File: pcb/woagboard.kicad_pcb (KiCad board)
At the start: 2 copper layers, 134.6 x 108.6 mm, 74 parts, among them J10 Flash connection, J2 HRO_TYPE-C-31-M-14, J3 Battery JST, Q2 2N7002, SW1 SW_Push, SW10 SW_Push, SW11 SW_Push, SW12 SW_Push, SW13 SW_Push, SW14 SW_Push, SW15 SW_Push, SW16 SW_Push, SW17 SW_Push, SW18 SW_Push, SW2 SW_Push, SW3 SW_Push, SW4 SW_Push, SW5 SW_Push, SW6 SW_Push, SW7 SW_Push, SW8 SW_Push, SW9 SW_Push, U1 SRV05-4, U10 MAX17048, U3 BQ24075, U9 nRF52840_E73-2G4M08S1C, Y1 32.768 KHz

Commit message: wip: finish left half and start work on right half
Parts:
- removed C17: 100n, Capacitor_SMD:C_0402_1005Metric
- removed D1, D10, D11, D12, D13, D14, D15, D16, D17, D18, D2, D3, D4, D5, D6, D7, D8, D9: D, Diode_SMD:D_SOD-523
- removed DUSB1: BSD3C051V, Diode_SMD:D_SOD-523
- removed LED2: orange, LED_SMD:LED_0402_1005Metric
- removed R19: 5k1, Resistor_SMD:R_0402_1005Metric
- removed U10: MAX17048, Package_DFN_QFN:DFN-8-1EP_2x2mm_P0.5mm_EP0.7x1.3mm
- added C10: 12p, Capacitor_SMD:C_0402_1005Metric, F.Cu at (189.9, 124.5)
- added C2: 4u7, Capacitor_SMD:C_0402_1005Metric, F.Cu at (180.1, 124.5)
- added C3: 4u7, Capacitor_SMD:C_0402_1005Metric, F.Cu at (182.0, 124.5)
- added C4: 1u, Capacitor_SMD:C_0402_1005Metric, F.Cu at (184.0, 124.5)
- added C8: 4u7, Capacitor_SMD:C_0402_1005Metric, F.Cu at (186.0, 124.5)
- added C9: 12p, Capacitor_SMD:C_0402_1005Metric, F.Cu at (187.9, 124.5)
- added F2: 750 mA, Fuse:Fuse_0603_1608Metric, F.Cu at (225.8, 128.5)
- added G***: LOGO, LOGO, F.Cu at (135.8, 43.5)
- added J1: Battery JST, Connector_JST:JST_PH_S2B-PH-K_1x02_P2.00mm_Horizontal, F.Cu at (203.3, 121.8)
- added L4: 10 uH, Inductor_SMD:L_0603_1608Metric, F.Cu at (228.3, 128.5)
- added Q1: 2N7002, Package_TO_SOT_SMD:SOT-23, F.Cu at (226.9, 124.1)
- added R14: 10k, Resistor_SMD:R_0402_1005Metric, F.Cu at (201.9, 126.2)
- added R15: 10k, Resistor_SMD:R_0402_1005Metric, F.Cu at (203.9, 126.2)
- added R16: 47k, Resistor_SMD:R_0402_1005Metric, F.Cu at (205.9, 126.2)
- added R17: 1k5, Resistor_SMD:R_0402_1005Metric, F.Cu at (207.9, 126.2)
- added R5: 5k1, Resistor_SMD:R_0402_1005Metric, F.Cu at (203.9, 129.1)
- added R6: 5k1, Resistor_SMD:R_0402_1005Metric, F.Cu at (205.9, 129.1)
- added R8: 100k, Resistor_SMD:R_0402_1005Metric, F.Cu at (207.9, 129.1)
- added RST2: RST, Jumper:SolderJumper-2_P1.3mm_Open_Pad1.0x1.5mm, F.Cu at (219.2, 128.4)
- added SW19: SW_Push, PCM_marbastlib-choc:SW_choc_v1_HS_CPG135001S30_1u, B.Cu at (179.6, 39.3)
- added SW20: SW_Push, PCM_marbastlib-choc:SW_choc_v1_HS_CPG135001S30_1u, B.Cu at (197.5, 36.7)
- added SW21: SW_Push, PCM_marbastlib-choc:SW_choc_v1_HS_CPG135001S30_1u, B.Cu at (215.5, 34.1)
- added SW22: SW_Push, PCM_marbastlib-choc:SW_choc_v1_HS_CPG135001S30_1u, B.Cu at (237.9, 40.1)
- added SW23: SW_Push, PCM_marbastlib-choc:SW_choc_v1_HS_CPG135001S30_1u, B.Cu at (260.6, 57.7)
- added SW24: SW_Push, PCM_marbastlib-choc:SW_choc_v1_HS_CPG135001S30_1u, B.Cu at (180.2, 56.3)
- added SW25: SW_Push, PCM_marbastlib-choc:SW_choc_v1_HS_CPG135001S30_1u, B.Cu at (198.1, 53.7)
- added SW26: SW_Push, PCM_marbastlib-choc:SW_choc_v1_HS_CPG135001S30_1u, B.Cu at (216.0, 51.1)
- added SW27: SW_Push, PCM_marbastlib-choc:SW_choc_v1_HS_CPG135001S30_1u, B.Cu at (237.0, 57.1)
- added SW28: SW_Push, PCM_marbastlib-choc:SW_choc_v1_HS_CPG135001S30_1u, B.Cu at (258.0, 74.5)
- added SW29: SW_Push, PCM_marbastlib-choc:SW_choc_v1_HS_CPG135001S30_1u, B.Cu at (180.8, 73.3)
- added SW30: SW_Push, PCM_marbastlib-choc:SW_choc_v1_HS_CPG135001S30_1u, B.Cu at (198.7, 70.7)
- added SW31: SW_Push, PCM_marbastlib-choc:SW_choc_v1_HS_CPG135001S30_1u, B.Cu at (216.6, 68.1)
- added SW32: SW_Push, PCM_marbastlib-choc:SW_choc_v1_HS_CPG135001S30_1u, B.Cu at (236.1, 74.1)
- added SW33: SW_Push, PCM_marbastlib-choc:SW_choc_v1_HS_CPG135001S30_1u, B.Cu at (255.3, 91.3)
- added SW34: SW_Push, PCM_marbastlib-choc:SW_choc_v1_HS_CPG135001S30_1u, B.Cu at (161.7, 111.0)
- added SW35: SW_Push, PCM_marbastlib-choc:SW_choc_v1_HS_CPG135001S30_1u, B.Cu at (179.7, 100.8)
- added SW36: SW_Push, PCM_marbastlib-choc:SW_choc_v1_HS_CPG135001S30_1u, B.Cu at (199.6, 95.7)
- added SWPL2: PWR, PCM_marbastlib-various:SW_MSK12C02-HB, F.Cu at (151.2, 75.5)
- added U2: SRV05-4, Package_TO_SOT_SMD:SOT-23-6, F.Cu at (219.8, 118.3)
- added U4: BQ24075, Package_DFN_QFN:VQFN-16-1EP_3x3mm_P0.5mm_EP1.6x1.6mm, F.Cu at (220.1, 123.5)
- added U5: nRF52840_E73-2G4M08S1C, PCM_marbastlib-various:nRF52840_E73-2G4M08S1C, F.Cu at (158.9, 56.0)
- added USB1: TYPE-C 16PIN 2MD(073), easyeda2kicad:USB-C-SMD_TYPE-C-6PIN-2MD-073, F.Cu at (130.2, 29.5)
- added USB2: TYPE-C 16PIN 2MD(073), easyeda2kicad:USB-C-SMD_TYPE-C-6PIN-2MD-073, F.Cu at (158.5, 29.6)
- added WOAG1: SHIELDNET, Jumper:SolderJumper-2_P1.3mm_Bridged2Bar_RoundedPad1.0x1.5mm, F.Cu at (123.0, 32.8)
- added WOAG2: SHIELDNET, Jumper:SolderJumper-2_P1.3mm_Bridged2Bar_RoundedPad1.0x1.5mm, F.Cu at (165.2, 33.2)
- added Y2: 32.768 KHz, Crystal:Crystal_SMD_2012-2Pin_2.0x1.2mm, F.Cu at (226.0, 119.8)
- C1: value 100n -> 4u7
- C13, R11, R12, R13, R9, U3: moved to F.Cu
- J2: value HRO_TYPE-C-31-M-14 -> Flash connection; footprint Connector_USB:USB_C_Receptacle_HRO_TYPE-C-31-M-12 -> Connector_PinHeader_2.54mm:PinHeader_1x05_P2.54mm_Vertical
- J3: footprint Connector_JST:JST_PH_S2B-PH-SM4-TB_1x02-1MP_P2.00mm_Horizontal -> Connector_JST:JST_PH_S2B-PH-K_1x02_P2.00mm_Horizontal
- R10: value 1k5 -> 100R; moved to F.Cu
- R18: value 5k1 -> 3k9
- RST1: renamed from SWRST1; footprint PCM_marbastlib-various:SW_SPST_SKQG_WithStem -> Jumper:SolderJumper-2_P1.3mm_Open_Pad1.0x1.5mm
- moved L2 109.1 mm to (201.9, 129.1), turned to 90 degrees
- moved SW12 102.5 mm to (52.5, 74.0), turned to 3 degrees
- moved J2 101.7 mm to (179.4, 128.2), turned to 90 degrees
- moved R10 96.8 mm to (209.9, 129.1), turned to 90 degrees
- moved C1 91.0 mm to (178.1, 124.5), turned to 90 degrees
- moved SW7 89.0 mm to (51.6, 57.1), turned to 3 degrees
- moved SW11 85.7 mm to (33.3, 91.2), turned to 9 degrees
- moved U9 84.7 mm to (129.8, 55.5), turned to -90 degrees
- moved SW2 82.4 mm to (50.7, 40.1), turned to 3 degrees
- moved Y1 79.8 mm to (118.6, 51.9), turned to 90 degrees
- moved SW18 75.4 mm to (126.9, 110.9), turned to 143 degrees
- moved SW17 72.2 mm to (108.9, 100.8), turned to -22 degrees
- moved C16 71.4 mm to (118.6, 53.9), turned to 180 degrees
- moved SW4 71.2 mm to (91.1, 36.6), turned to -2 degrees
- moved C15 70.5 mm to (118.9, 49.9), turned to 180 degrees
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- renumbered SW13 to SW1, SW8 to SW10, SW15 to SW11, SW18 to SW12, SW1 to SW13, SW4 to SW14, SW7 to SW15, SW10 to SW16, SW11 to SW17, SW12 to SW18, SW16 to SW2, SW6 to SW4, SW9 to SW5, SW14 to SW6, SW17 to SW7, SW2 to SW8, SW5 to SW9
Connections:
- C1 pad 1: Earth -> +5V
- L2 pad 1: Earth -> VBUS
- L2 pad 2: GND -> Net-(F2-Pad1)
- R1 pad 1: GNDPWR -> Net-(USB1-CC2)
- R1 pad 2: Net-(J2-CC2) -> GND
- R10 pad 1: Net-(LED2-K) -> +5V
- R10 pad 2: Net-(U3-~{CHG}) -> Net-(Q1-G)
- R18 pad 1: SDA -> Net-(U4-ISET)
- R18 pad 2: VDD -> GND
- R2 pad 1: GNDPWR -> GND
- R2 pad 2: Net-(J2-CC1) -> Net-(USB1-CC1)
- SW1 pad 1: C2 -> Switch1
- SW1 pad 2: Net-(D13-A) -> GND
- SW10 pad 1: C2 -> Switch10
- SW10 pad 2: Net-(D8-A) -> GND
- SW11 pad 1: C4 -> Switch11
- SW11 pad 2: Net-(D15-A) -> GND
- SW12 pad 1: C4 -> Switch12
- SW12 pad 2: Net-(D18-A) -> GND
- SW13 pad 1: C0 -> Switch13
- SW13 pad 2: Net-(D1-A) -> GND
- SW14 pad 1: C3 -> Switch14
- SW14 pad 2: Net-(D4-A) -> GND
- SW15 pad 1: C1 -> Switch15
- SW15 pad 2: Net-(D7-A) -> GND
- SW16 pad 1: C4 -> Switch16
- SW16 pad 2: Net-(D10-A) -> GND
- SW17 pad 1: C0 -> Switch17
- SW17 pad 2: Net-(D11-A) -> GND
- SW18 pad 1: C1 -> Switch18
- SW18 pad 2: Net-(D12-A) -> GND
- SW2 pad 1: C2 -> Switch2
- SW2 pad 2: Net-(D16-A) -> GND
- SW3 pad 1: C2 -> Switch3
- SW3 pad 2: Net-(D3-A) -> GND
- SW4 pad 1: C0 -> Switch4
- SW4 pad 2: Net-(D6-A) -> GND
- SW5 pad 1: C3 -> Switch5
- SW5 pad 2: Net-(D9-A) -> GND
- SW6 pad 1: C3 -> Switch6
- SW6 pad 2: Net-(D14-A) -> GND
- SW7 pad 1: C3 -> Switch7
- SW7 pad 2: Net-(D17-A) -> GND
- SW8 pad 1: C1 -> Switch8
- SW8 pad 2: Net-(D2-A) -> GND
- SW9 pad 1: C4 -> Switch9
- SW9 pad 2: Net-(D5-A) -> GND
- U3 pad 9: Net-(U3-~{CHG}) -> unconnected-(U3-~{CHG}-Pad9)
- U9 pad 10: unconnected-(U9-P0.30/AIN6-Pad10) -> Switch1
- U9 pad 12: unconnected-(U9-P0.26-Pad12) -> Switch6
- U9 pad 14: unconnected-(U9-P0.06-Pad14) -> Switch7
- U9 pad 15: SCL -> unconnected-(U9-P0.05/AIN3-Pad15)
- U9 pad 16: unconnected-(U9-P0.08-Pad16) -> Switch8
- U9 pad 17: R3 -> unconnected-(U9-P1.09-Pad17)
- U9 pad 18: C2 -> Switch9
- U9 pad 20: unconnected-(U9-P0.12-Pad20) -> Switch10
- U9 pad 22: SDA -> Switch11
- U9 pad 28: unconnected-(U9-P0.15-Pad28) -> Switch12
- U9 pad 3: C1 -> unconnected-(U9-P0.03/AIN1-Pad3)
- U9 pad 30: unconnected-(U9-P0.17-Pad30) -> Switch13
- U9 pad 32: unconnected-(U9-P0.20-Pad32) -> Switch14
- U9 pad 33: unconnected-(U9-P0.13-Pad33) -> Switch16
- U9 pad 34: UG_LV -> Switch15
- U9 pad 35: unconnected-(U9-P0.24-Pad35) -> Switch18
- U9 pad 36: UG_EN -> Switch17
- U9 pad 38: R0 -> unconnected-(U9-P1.02-Pad38)
- U9 pad 4: C3 -> unconnected-(U9-P0.28/AIN4-Pad4)
- U9 pad 40: R1 -> unconnected-(U9-P1.04-Pad40)
- U9 pad 42: R2 -> unconnected-(U9-P1.06-Pad42)
- U9 pad 6: unconnected-(U9-P1.13-Pad6) -> Switch5
- U9 pad 7: C0 -> Switch4
- U9 pad 8: C4 -> Switch3
- U9 pad 9: unconnected-(U9-P0.31/AIN7-Pad9) -> Switch2
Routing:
- net C0: track 152.0 -> 0.00 mm
- net C1: track 152.0 -> 0.00 mm
- net C2: track 152.0 -> 0.00 mm
- net C3: track 152.0 -> 0.00 mm
- net C4: track 133.0 -> 0.00 mm
- net Switch6: track 0.00 -> 112.2 mm, vias 0 -> 1
- net Switch11: track 0.00 -> 107.1 mm, vias 0 -> 1
- net Switch1: track 0.00 -> 97.3 mm, vias 0 -> 1
- net +5V: track 3.08 -> 90.8 mm, vias 0 -> 3
- net Switch12: track 0.00 -> 78.7 mm, vias 0 -> 1
- net Switch7: track 0.00 -> 77.7 mm, vias 0 -> 1
- net Switch2: track 0.00 -> 72.9 mm, vias 0 -> 1
- net USB-D+: track 131.4 -> 58.8 mm, vias 2 -> 0
- net USB-D-: track 126.8 -> 60.1 mm, vias 2 -> 0
- net Switch17: track 0.00 -> 53.6 mm, vias 0 -> 3
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- added copper zone on B.Cu, net GND
- added copper zone on F.Cu, net GND
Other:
- board size 134.6 x 108.6 mm -> 252.9 x 99.4 mm
- board text added: "GND"
- board text added: "NOISE IS CALLING PICK UP PHONE"
- board text added: "RST"
- board text added: "SWDCLK"
- board text added: "SWDIO"
- board text added: "VDD"
- board text added: "WOAG BOARD"

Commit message: wip: initial pcb of full woagboard
note: Do not print this. It's not even close to ready probably
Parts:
- removed Q1, Q2: 2N7002, Package_TO_SOT_SMD:SOT-23
- removed R10: 100R, Resistor_SMD:R_0402_1005Metric
- removed R14, R7: 10k, Resistor_SMD:R_0402_1005Metric
- removed R8: 100k, Resistor_SMD:R_0402_1005Metric
- removed SWPL1, SWPL2: PWR, PCM_marbastlib-various:SW_MSK12C02-HB
- added LED1: Orange, LED_SMD:LED_0805_2012Metric, F.Cu at (133.5, 73.0)
- added LED2: Orange, LED_SMD:LED_0805_2012Metric, F.Cu at (149.5, 73.2)
- added Snap1: 5.5mm, PCM_marbastlib-various:mousebites_5p5mm_easysnap, F.Cu at (144.6, 95.2)
- added Snap2: 5.5mm, PCM_marbastlib-various:mousebites_5p5mm_easysnap, F.Cu at (144.6, 38.2)
- added kibuzzard-66E410C5: G***, kibuzzard-66E410C5, F.Cu at (128.1, 43.7)
- J1: moved to B.Cu
- R13, R18: footprint Resistor_SMD:R_0402_1005Metric -> Resistor_SMD:R_0603_1608Metric
- R3: value 100k -> 1k5
- R4: value 100R -> 1k5
- RST1, RST2: value RST -> EVQ-P7C01P; footprint Jumper:SolderJumper-2_P1.3mm_Open_Pad1.0x1.5mm -> EVQ-P7C01P:SW_EVQ-P7C01P
- moved F2 118.6 mm to (149.8, 37.5), turned to 0 degrees
- moved R6 108.9 mm to (150.6, 35.2), turned to -90 degrees
- moved L2 107.7 mm to (149.1, 35.2), turned to -90 degrees
- moved U2 105.8 mm to (153.6, 35.9), turned to 180 degrees
- moved R5 104.9 mm to (157.6, 35.0)
- moved L4 98.8 mm to (165.6, 52.2), turned to -90 degrees
- moved RST2 91.2 mm to (146.5, 73.2), turned to -90 degrees
- moved Y2 85.5 mm to (165.1, 59.7), turned to -90 degrees
- moved C8 80.8 mm to (161.3, 47.5)
- moved U4 80.8 mm to (158.4, 71.3)
- moved R17 77.2 mm to (157.0, 68.2), turned to 180 degrees
- moved R18 77.0 mm to (154.2, 73.0), turned to 180 degrees
- moved R16 74.8 mm to (155.0, 71.5), turned to 180 degrees
- moved C4 72.2 mm to (166.5, 54.5), turned to 0 degrees
- moved C10 71.4 mm to (165.1, 57.5), turned to 0 degrees
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- renumbered J10 to J4
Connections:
- R3 pad 2: +BATT -> Net-(U3-~{CHG})
- R4 pad 1: +5V -> Net-(LED2-K)
- R4 pad 2: Net-(Q2-G) -> Net-(U4-~{CHG})
- U3 pad 15: SYSOFF -> unconnected-(U3-SYSOFF-Pad15)
- U3 pad 9: unconnected-(U3-~{CHG}-Pad9) -> Net-(U3-~{CHG})
- U4 pad 15: SYSOFF-R -> unconnected-(U4-SYSOFF-Pad15)
- U4 pad 9: unconnected-(U4-~{CHG}-Pad9) -> Net-(U4-~{CHG})
- U5 pad 10: Switch19 -> Switch29
- U5 pad 12: Switch24 -> Switch30
- U5 pad 2: unconnected-(U5-P1.10-Pad2) -> Switch36
- U5 pad 22: Switch29 -> Switch23
- U5 pad 28: Switch30 -> Switch22
- U5 pad 3: unconnected-(U5-P0.03/AIN1-Pad3) -> Switch35
- U5 pad 30: Switch31 -> Switch21
- U5 pad 32: Switch32 -> Switch20
- U5 pad 33: Switch34 -> unconnected-(U5-P0.13-Pad33)
- U5 pad 34: Switch33 -> Switch19
- U5 pad 35: Switch36 -> unconnected-(U5-P0.24-Pad35)
- U5 pad 36: Switch35 -> unconnected-(U5-P1.00-Pad36)
- U5 pad 4: unconnected-(U5-P0.28/AIN4-Pad4) -> Switch34
- U5 pad 6: Switch23 -> Switch33
- U5 pad 7: Switch22 -> Switch32
- U5 pad 8: Switch21 -> Switch31
- U5 pad 9: Switch20 -> Switch24
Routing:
- net Switch33: track 0.00 -> 119.9 mm, vias 0 -> 1
- net Switch28: track 0.00 -> 109.9 mm, vias 0 -> 1
- net Switch23: track 0.00 -> 98.2 mm, vias 0 -> 1
- net Switch32: track 0.00 -> 87.9 mm, vias 0 -> 1
- net Switch27: track 0.00 -> 77.3 mm, vias 0 -> 1
- net Switch34: track 0.00 -> 74.9 mm, vias 0 -> 1
- net Switch22: track 0.00 -> 72.5 mm, vias 0 -> 1
- net Switch31: track 0.00 -> 67.7 mm, vias 0 -> 1
- net +VSW: track 36.6 -> 97.0 mm, vias 2 -> 5
- net GND: track 70.3 -> 128.9 mm, vias 8 -> 15
- net Switch21: track 0.00 -> 58.3 mm, vias 0 -> 1
- net Switch26: track 0.00 -> 54.5 mm, vias 0 -> 1
- net Switch35: track 0.00 -> 51.6 mm, vias 0 -> 1
- net Switch36: track 0.00 -> 50.5 mm, vias 0 -> 1
- net Switch30: track 0.00 -> 48.3 mm, vias 0 -> 1
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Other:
- board size 252.9 x 99.4 mm -> 247.7 x 97.6 mm
- board text removed: "WOAG BOARD"

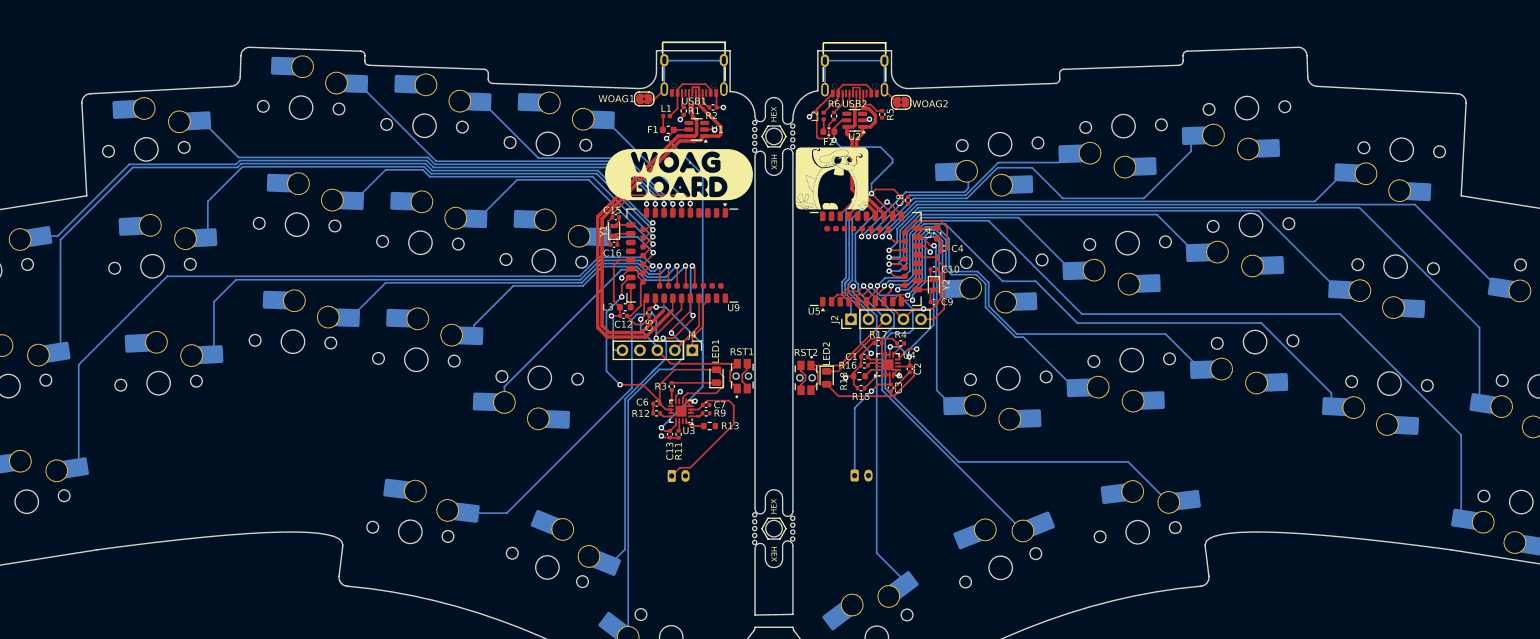
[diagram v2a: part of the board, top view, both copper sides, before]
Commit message: fix: much better routing
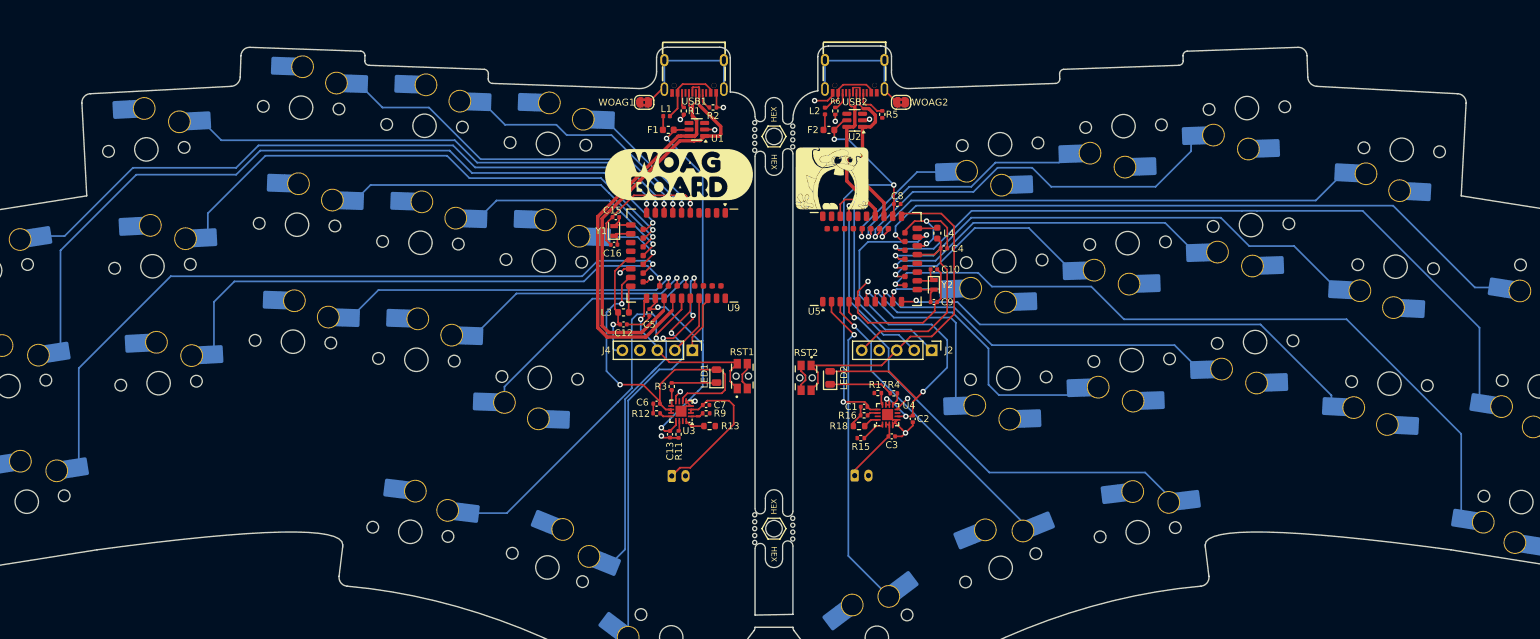
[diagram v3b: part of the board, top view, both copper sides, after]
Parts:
- moved J2 12.6 mm to (164.8, 69.2), turned to -90 degrees
- moved R4 7.32 mm to (159.2, 75.5)
- moved C2 7.26 mm to (162.0, 79.2)
- moved C1 7.25 mm to (154.9, 77.5)
- moved R15 7.25 mm to (154.4, 82.0)
- moved R16 7.25 mm to (154.9, 78.7)
- moved R17 7.25 mm to (156.9, 75.5)
- moved R18 7.25 mm to (154.2, 80.2)
- moved U4 7.25 mm to (158.3, 78.6)
- moved C3 7.05 mm to (158.9, 81.8), turned to 0 degrees
- moved C8 1.65 mm to (159.8, 48.0), turned to 0 degrees
- moved C12 1.25 mm to (120.0, 65.5)
- moved L3 0.79 mm to (120.0, 63.8)
- moved L2 0.77 mm to (149.2, 34.5)
- moved R6 0.77 mm to (150.8, 34.5)
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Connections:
- U5 pad 10: Switch29 -> Switch32
- U5 pad 12: Switch30 -> Switch33
- U5 pad 6: Switch33 -> Switch29
- U5 pad 7: Switch32 -> Switch30
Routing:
- net +VSW: track 97.0 -> 120.4 mm, vias 5 -> 6
- net GND: track 128.9 -> 110.4 mm, vias 15 -> 17
- net Switch32: track 87.9 -> 69.8 mm
- net Switch31: track 67.7 -> 51.8 mm
- net Switch33: track 119.9 -> 106.3 mm
- net Switch24: track 22.9 -> 9.59 mm
- net Switch34: track 74.9 -> 61.9 mm
- net SWDCLK-R: track 21.6 -> 33.4 mm
- net VDD: track 36.5 -> 46.8 mm
- net Switch29: track 38.6 -> 28.4 mm
- net +BATT: track 40.9 -> 32.4 mm, vias 1 -> 0
- net Switch30: track 48.3 -> 40.2 mm
- net Switch35: track 51.6 -> 44.3 mm
- net RST-R: track 42.5 -> 49.6 mm, vias 1 -> 0
- net SWDIO-R: track 20.8 -> 27.8 mm
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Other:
- board size 247.7 x 97.6 mm -> 247.7 x 97.7 mm

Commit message: pcb: more pcb design and silkscreen shenanigains
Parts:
- added G***: LOGO, LOGO, B.Cu at (158.3, 89.3)
- moved J1 40.8 mm to (194.1, 82.2), turned to -90 degrees
- moved J3 35.6 mm to (91.5, 84.2), turned to 90 degrees
- moved kibuzzard-66E410C5 0.80 mm to (127.2, 43.7)
- moved R4 0.75 mm to (159.2, 74.8)
- moved R17 0.73 mm to (156.8, 74.8)
- moved G*** 0.47 mm to (150.8, 44.2)
- moved L3 0.25 mm to (119.8, 63.8)
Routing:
- net +BATT: track 32.4 -> 95.8 mm
- net Switch16: track 55.4 -> 53.8 mm
- net Switch18: track 55.4 -> 54.0 mm
- net +VSW: track 120.4 -> 121.5 mm
- net +5V: track 134.6 -> 135.6 mm
- net SWDIO-R: track 27.8 -> 28.6 mm
- net /ILIM: track 3.56 -> 4.34 mm
- net Net-(U4-~{CHG}): track 1.94 -> 2.69 mm
- net USB-D+: track 58.8 -> 59.5 mm
- net USB-D-: track 60.8 -> 61.5 mm
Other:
- board text added: "BIGDIE"
- board text added: "PROTOCOL 3: PROTECT THE NOISE"
- board text added: "yeag"

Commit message: chore: move some traces
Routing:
- net +5V: track 135.6 -> 133.3 mm
- net Switch11: track 106.4 -> 108.4 mm
- net Switch7: track 78.0 -> 76.3 mm
- net Switch29: track 28.4 -> 27.1 mm
- net Switch25: track 32.4 -> 31.6 mm
- net Switch26: track 49.4 -> 48.8 mm
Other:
- board text added: "ඞ"
